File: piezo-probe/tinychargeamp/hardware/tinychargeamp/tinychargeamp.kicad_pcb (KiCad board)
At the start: 2 copper layers, 23.5 x 15.9 mm, 9 parts, among them J1 Conn_01x02, J2 Conn_01x03, J3 Conn_01x02, U1 ATtiny13A-SSU

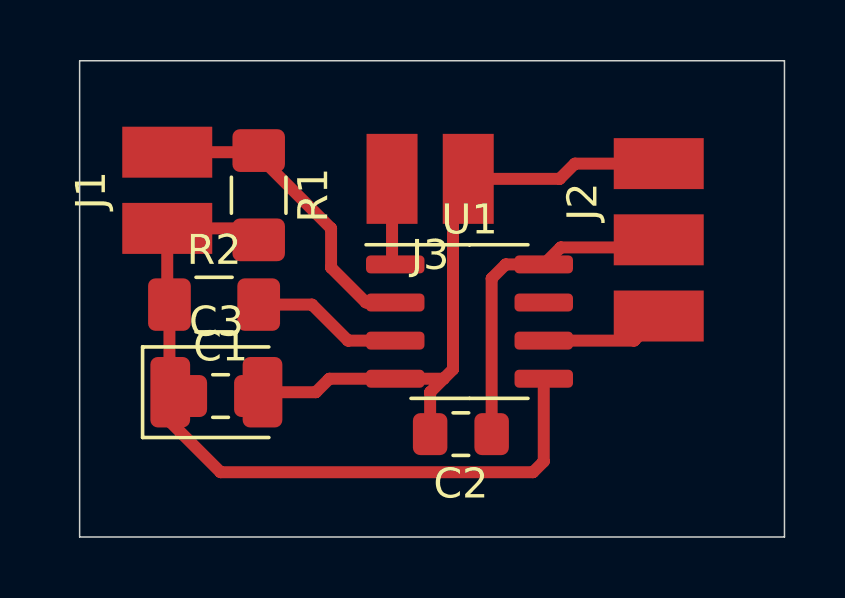
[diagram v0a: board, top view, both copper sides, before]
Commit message: Update board and firmware
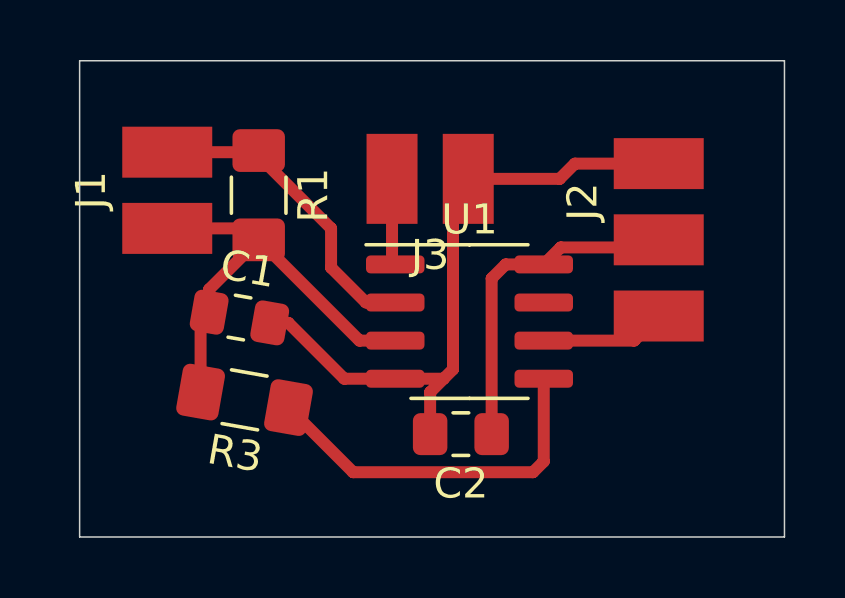
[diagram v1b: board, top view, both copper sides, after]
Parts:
- removed C3: 100u, Capacitor_Tantalum_SMD:CP_EIA-3528-15_AVX-H
- removed R2: ?, Resistor_SMD:R_1206_3216Metric_Pad1.42x1.75mm_HandSolder
- added R3: 22k, Resistor_SMD:R_1206_3216Metric_Pad1.42x1.75mm_HandSolder, F.Cu at (24.4, 28.6)
- R1: value 1meg -> 120k
- moved C1 2.69 mm to (24.3, 25.8), turned to 350 degrees
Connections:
- U1 pad 3: /REFGEN -> /PIEZO-
- U1 pad 5: /PIEZO- -> Net-(R3-Pad1)
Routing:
- net Net-(R3-Pad1): track 0.00 -> 12.3 mm
- net /PIEZO-: track 25.7 -> 15.0 mm
- net /REFGEN: track 5.05 -> 0.00 mm
